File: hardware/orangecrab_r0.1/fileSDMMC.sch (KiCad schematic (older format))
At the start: 1 part, among them J4 MicroSD

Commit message: Update schematic
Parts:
- J4: symbol bosonFrameGrabber-rescue:Conn_01x11_Male-conn -> Connector:Conn_01x11_Male
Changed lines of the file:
@@
 $Descr A4 11693 8268
 encoding utf-8
-Sheet 4 5
+Sheet 4 6
 Title ""
 Date ""
@@
 $EndComp
 $Comp
-L bosonFrameGrabber-rescue:Conn_01x11_Male-conn J4
+L Connector:Conn_01x11_Male J4
 U 1 1 5AC0A68B
 P 5650 3850

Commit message: Routed more FPGA signals
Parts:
- J4: footprint bosonFrameGrabber:1040310811 -> gkl_conn:molex_microsd_1040310811
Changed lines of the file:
@@
 F 0 "J4" H 5450 4600 50  0000 C CNN
 F 1 "MicroSD" H 5400 4500 50  0000 C CNN
-F 2 "bosonFrameGrabber:1040310811" H 5650 3850 50  0001 C CNN
+F 2 "gkl_conn:molex_microsd_1040310811" H 5650 3850 50  0001 C CNN
 F 3 "~" H 5650 3850 50  0001 C CNN
 F 4 " WM6357CT-ND" H 5650 3850 60  0001 C CNN "SN-DK"

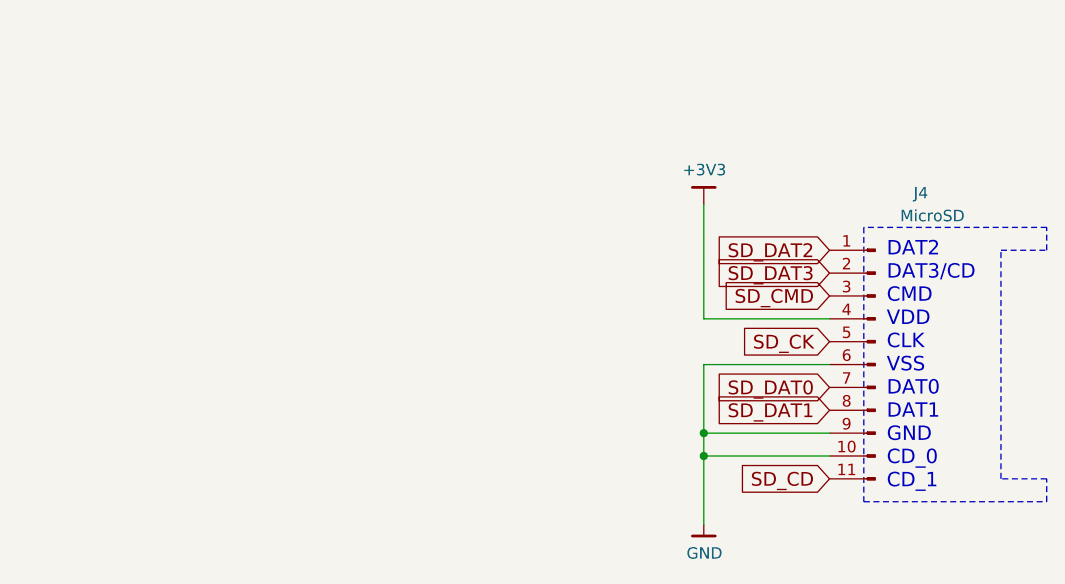
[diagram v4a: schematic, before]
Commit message: Added loads of decoupling capacitors. Added SD card. Started planning out power plane
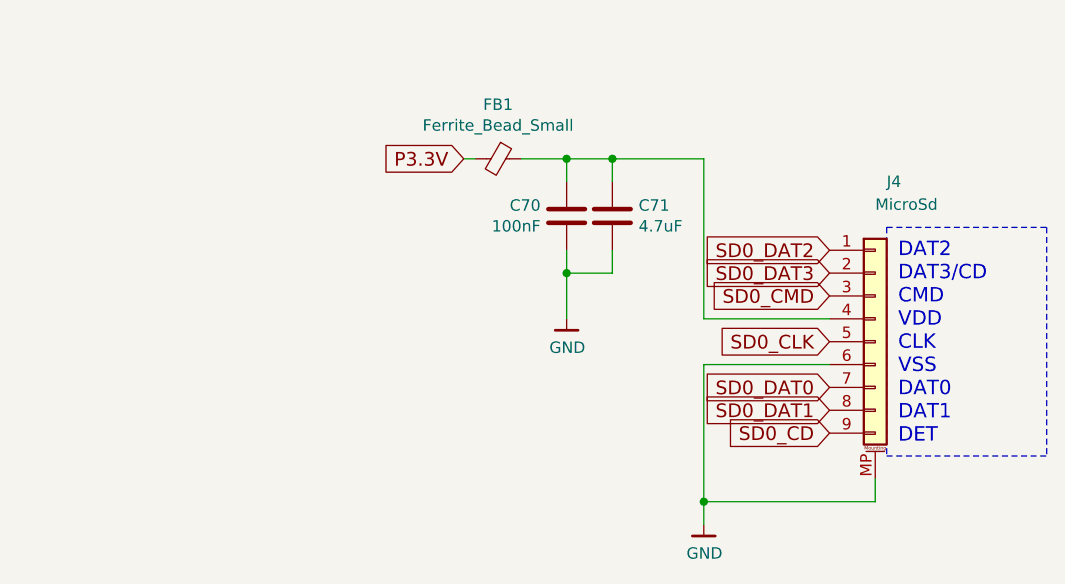
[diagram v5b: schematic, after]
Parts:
- removed J4: MicroSD, gkl_conn:molex_microsd_1040310811, symbol Connector:Conn_01x11_Male
- added C70: 100nF, Capacitor_SMD:C_0201_0603Metric, symbol Device:C
- added C71: 4.7uF, Capacitor_SMD:C_0603_1608Metric, symbol Device:C
- added FB1: Ferrite_Bead_Small, Inductor_SMD:L_0402_1005Metric, symbol Device:Ferrite_Bead_Small
- added J4: MicroSd, gkl_conn:micro_sd_1051620001, symbol Connector_Generic_MountingPin:Conn_01x09_MountingPin
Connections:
- net GND: now also C70.1, C71.2, J4.6 (Pin_6), J4.MP (MountPin)
- new net: C70.2, C71.1, FB1.1, J4.4 (Pin_4)
- new net P3.3V: FB1.2
- new net SD0_CD: J4.9 (Pin_9)
- new net SD0_CLK: J4.5 (Pin_5)
- new net SD0_CMD: J4.3 (Pin_3)
- new net SD0_DAT0: J4.7 (Pin_7)
- new net SD0_DAT1: J4.8 (Pin_8)
- new net SD0_DAT2: J4.1 (Pin_1)
- new net SD0_DAT3: J4.2 (Pin_2)
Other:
- note added: "DAT2\nDAT3/CD\nCMD\nVDD\nCLK\nVSS\nDAT0\nDAT1\nDET"
- note removed: "DAT2\nDAT3/CD\nCMD\nVDD\nCLK\nVSS\nDAT0\nDAT1\nGND\nCD_0\nCD_1\n"
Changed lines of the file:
@@
 $Descr A4 11693 8268
 encoding utf-8
-Sheet 4 6
+Sheet 4 7
 Title "Orange Crab"
 Date "2019-06-28"
@@
 $EndDescr
 Text GLabel 5450 3950 0    60   Input ~ 0
-SD_DAT0
+SD0_DAT0
 Text GLabel 5450 4050 0    60   Input ~ 0
-SD_DAT1
+SD0_DAT1
 Text GLabel 5450 3350 0    60   Input ~ 0
-SD_DAT2
+SD0_DAT2
 Text GLabel 5450 3450 0    60   Input ~ 0
-SD_DAT3
+SD0_DAT3
 Text GLabel 5450 3550 0    60   Input ~ 0
-SD_CMD
+SD0_CMD
 Text GLabel 5450 3750 0    60   Input ~ 0
-SD_CK
-Text GLabel 5450 4350 0    60   Input ~ 0
-SD_CD
-$Comp
-L gkl_power:+3V3 #PWR049
-U 1 1 5AC0A2E2
-P 4900 3150
-F 0 "#PWR049" H 4900 3000 50  0001 C CNN
-F 1 "+3V3" H 4903 3301 50  0000 C CNN
-F 2 "" H 4900 3150 50  0001 C CNN
-F 3 "" H 4900 3150 50  0001 C CNN
-	1    4900 3150
-	1    0    0    -1
-$EndComp
+SD0_CLK
+Text GLabel 5450 4150 0    60   Input ~ 0
+SD0_CD
 $Comp
 L gkl_power:GND #PWR050
@@
 	1    0    0    -1
 $EndComp
-$Comp
-L Connector:Conn_01x11_Male J4
-U 1 1 5AC0A68B
-P 5650 3850
-F 0 "J4" H 5450 4600 50  0000 C CNN
-F 1 "MicroSD" H 5400 4500 50  0000 C CNN
-F 2 "gkl_conn:molex_microsd_1040310811" H 5650 3850 50  0001 C CNN
-F 3 "~" H 5650 3850 50  0001 C CNN
-F 4 " WM6357CT-ND" H 5650 3850 60  0001 C CNN "SN-DK"
-F 5 "1040310811" H 0   0   50  0001 C CNN "PN"
-	1    5650 3850
-	-1   0    0    -1
-$EndComp
-Wire Wire Line
-	4900 3850 4900 4150
-Wire Wire Line
-	4900 4150 5450 4150
-Text Notes 5700 4400 0    63   ~ 0
-DAT2\nDAT3/CD\nCMD\nVDD\nCLK\nVSS\nDAT0\nDAT1\nGND\nCD_0\nCD_1\n
+Text Notes 5750 4200 0    63   ~ 0
+DAT2\nDAT3/CD\nCMD\nVDD\nCLK\nVSS\nDAT0\nDAT1\nDET
 Wire Notes Line
-	5600 3250 5600 4450
-Wire Notes Line
-	5600 4450 6400 4450
-Wire Notes Line
-	6400 4450 6400 4350
-Wire Notes Line
-	6400 4350 6200 4350
-Wire Notes Line
-	6200 4350 6200 3350
-Wire Notes Line
-	6200 3350 6400 3350
-Wire Notes Line
-	6400 3350 6400 3250
-Wire Notes Line
-	6400 3250 5600 3250
+	5700 3250 5700 4250
 Wire Wire Line
 	5450 3650 4900 3650
 Wire Wire Line
-	4900 3650 4900 3150
+	5450 3850 4900 3850
+$Comp
+L Connector_Generic_MountingPin:Conn_01x09_MountingPin J4
+U 1 1 5D5BA533
+P 5650 3750
+F 0 "J4" H 5700 4450 50  0000 L CNN
+F 1 "MicroSd" H 5650 4350 50  0000 L CNN
+F 2 "gkl_conn:micro_sd_1051620001" H 5650 3750 50  0001 C CNN
+F 3 "~" H 5650 3750 50  0001 C CNN
+F 4 "1051620001" H 5650 3750 50  0001 C CNN "PN"
+F 5 "Molex" H 5650 3750 50  0001 C CNN "Mfg"
+	1    5650 3750
+	1    0    0    -1
+$EndComp
 Wire Wire Line
-	5450 3850 4900 3850
-Connection ~ 4900 4150
+	4900 3850 4900 4450
 Wire Wire Line
-	4900 4150 4900 4250
+	5650 4350 5650 4450
 Wire Wire Line
-	5450 4250 4900 4250
-Connection ~ 4900 4250
+	5650 4450 4900 4450
+Connection ~ 4900 4450
 Wire Wire Line
-	4900 4250 4900 4550
+	4900 4450 4900 4550
+Wire Notes Line
+	5700 4250 6400 4250
+Wire Notes Line
+	6400 3250 6400 4250
+Wire Notes Line
+	5700 3250 6400 3250
+Text GLabel 3850 2950 0    60   Input ~ 0
+P3.3V
+$Comp
+L Device:Ferrite_Bead_Small FB1
+U 1 1 5D5BE84B
+P 4000 2950
+F 0 "FB1" V 3763 2950 50  0000 C CNN
+F 1 "Ferrite_Bead_Small" V 3854 2950 50  0000 C CNN
+F 2 "Inductor_SMD:L_0402_1005Metric" V 3930 2950 50  0001 C CNN
+F 3 "~" H 4000 2950 50  0001 C CNN
+	1    4000 2950
+	0    1    1    0
+$EndComp
+$Comp
+L Device:C C71
+U 1 1 5D5BF142
+P 4500 3200
+F 0 "C71" H 4615 3246 50  0000 L CNN
+F 1 "4.7uF" H 4615 3155 50  0000 L CNN
+F 2 "Capacitor_SMD:C_0603_1608Metric" H 4538 3050 50  0001 C CNN
+F 3 "~" H 4500 3200 50  0001 C CNN
+	1    4500 3200
+	1    0    0    -1
+$EndComp
+$Comp
+L Device:C C70
+U 1 1 5D5BF444
+P 4300 3200
+F 0 "C70" H 4186 3154 50  0000 R CNN
+F 1 "100nF" H 4186 3245 50  0000 R CNN
+F 2 "Capacitor_SMD:C_0201_0603Metric" H 4338 3050 50  0001 C CNN
+F 3 "~" H 4300 3200 50  0001 C CNN
+	1    4300 3200
+	1    0    0    1
+$EndComp
+Wire Wire Line
+	4100 2950 4300 2950
+Wire Wire Line
+	4900 2950 4900 3650
+Wire Wire Line
+	4500 3050 4500 2950
+Connection ~ 4500 2950
+Wire Wire Line
+	4500 2950 4900 2950
+Wire Wire Line
+	4300 3050 4300 2950
+Connection ~ 4300 2950
+Wire Wire Line
+	4300 2950 4500 2950
+Wire Wire Line
+	3900 2950 3850 2950
+Wire Wire Line
+	4300 3350 4300 3450
+Wire Wire Line
+	4500 3350 4500 3450
+Wire Wire Line
+	4500 3450 4300 3450
+Connection ~ 4300 3450
+Wire Wire Line
+	4300 3450 4300 3650
+$Comp
+L gkl_power:GND #PWR0159
+U 1 1 5D5C1FC1
+P 4300 3650
+F 0 "#PWR0159" H 4300 3400 50  0001 C CNN
+F 1 "GND" H 4303 3524 50  0000 C CNN
+F 2 "" H 4200 3300 50  0001 C CNN
+F 3 "" H 4300 3650 50  0001 C CNN
+	1    4300 3650
+	1    0    0    -1
+$EndComp
 $EndSCHEMATC

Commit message: Added pulldown on TS pin to disable TS func. Added 4.7uF cap to USB input. Corrected Battery polarity Calculated correct DCDC Fb Added pullup to SWCLK Added Pulldown to TCK Added Pinout legend on top layer Fixed Missing VCC on Flash Neaten up Power Plane Schematic Checklist complete.
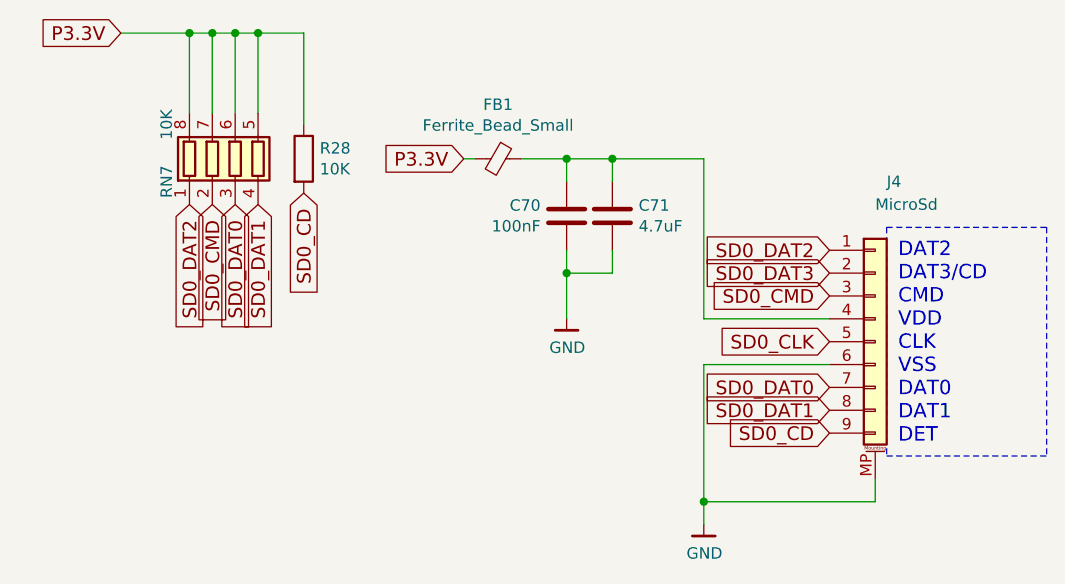
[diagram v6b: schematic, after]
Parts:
- added R28: 10K, Resistor_SMD:R_0201_0603Metric, symbol Device:R
- added RN7: 10K, Resistor_SMD:R_Array_Convex_4x0402, symbol Device:R_Pack04
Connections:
- net P3.3V: now also R28.1, RN7.5 (R4.2), RN7.6 (R3.2), RN7.7 (R2.2), RN7.8 (R1.2)
- net SD0_CD: now also R28.2
- net SD0_CMD: now also RN7.2 (R2.1)
- net SD0_DAT0: now also RN7.3 (R3.1)
- net SD0_DAT1: now also RN7.4 (R4.1)
- net SD0_DAT2: now also RN7.1 (R1.1)
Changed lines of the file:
@@
 	1    0    0    -1
 $EndComp
+$Comp
+L Device:R_Pack04 RN?
+U 1 1 5D5ABE41
+P 2850 2950
+AR Path="/5ABD38F2/5D5ABE41" Ref="RN?"  Part="1"
+AR Path="/5AC0A2A0/5D5ABE41" Ref="RN7"  Part="1"
+F 0 "RN7" V 2550 2850 50  0000 C CNN
+F 1 "10K" V 2550 3100 50  0000 C CNN
+F 2 "Resistor_SMD:R_Array_Convex_4x0402" V 3125 2950 50  0001 C CNN
+F 3 "~" H 2850 2950 50  0001 C CNN
+F 4 "CRA06S08349R9FTA" H 2850 2950 50  0001 C CNN "PN"
+	1    2850 2950
+	1    0    0    -1
+$EndComp
+Text GLabel 2350 2400 0    60   Input ~ 0
+P3.3V
+Wire Wire Line
+	2350 2400 2650 2400
+Wire Wire Line
+	2650 2400 2650 2750
+Wire Wire Line
+	2650 2400 2750 2400
+Wire Wire Line
+	2750 2400 2750 2750
+Connection ~ 2650 2400
+Wire Wire Line
+	2750 2400 2850 2400
+Wire Wire Line
+	2850 2400 2850 2750
+Connection ~ 2750 2400
+Wire Wire Line
+	2850 2400 2950 2400
+Wire Wire Line
+	2950 2400 2950 2750
+Connection ~ 2850 2400
+Text GLabel 2650 3150 3    60   Input ~ 0
+SD0_DAT2
+Text GLabel 2750 3150 3    60   Input ~ 0
+SD0_CMD
+Text GLabel 2850 3150 3    60   Input ~ 0
+SD0_DAT0
+Text GLabel 2950 3150 3    60   Input ~ 0
+SD0_DAT1
+$Comp
+L Device:R R28
+U 1 1 5D5AD51E
+P 3150 2950
+F 0 "R28" H 3220 2996 50  0000 L CNN
+F 1 "10K" H 3220 2905 50  0000 L CNN
+F 2 "Resistor_SMD:R_0201_0603Metric" V 3080 2950 50  0001 C CNN
+F 3 "~" H 3150 2950 50  0001 C CNN
+	1    3150 2950
+	1    0    0    -1
+$EndComp
+Text GLabel 3150 3100 3    60   Input ~ 0
+SD0_CD
+Wire Wire Line
+	2950 2400 3150 2400
+Wire Wire Line
+	3150 2400 3150 2800
+Connection ~ 2950 2400
 $EndSCHEMATC

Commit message: Rerouted User Io to provide a common connector. Diff pairs routed. Updated gkl to include new connector. Removed old test points Removed JTAG test points on bottom layer. Moved micro SD card Moved some components to provide space for ul marking.
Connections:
- net SD0_CMD: now also RN7.3 (R3.1); no longer RN7.2 (R2.1)
- net SD0_DAT0: now also RN7.2 (R2.1); no longer RN7.3 (R3.1)
- net SD0_DAT1: now also RN7.1 (R1.1); no longer RN7.4 (R4.1)
- net SD0_DAT2: now also RN7.4 (R4.1); no longer RN7.1 (R1.1)
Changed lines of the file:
@@
 	2950 2400 2950 2750
 Connection ~ 2850 2400
+Text GLabel 2950 3150 3    60   Input ~ 0
+SD0_DAT2
+Text GLabel 2850 3150 3    60   Input ~ 0
+SD0_CMD
+Text GLabel 2750 3150 3    60   Input ~ 0
+SD0_DAT0
 Text GLabel 2650 3150 3    60   Input ~ 0
-SD0_DAT2
-Text GLabel 2750 3150 3    60   Input ~ 0
-SD0_CMD
-Text GLabel 2850 3150 3    60   Input ~ 0
-SD0_DAT0
-Text GLabel 2950 3150 3    60   Input ~ 0
 SD0_DAT1
 $Comp

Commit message: Updated BOM fields in KiCad project Exported ibom Clarify fab notes
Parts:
- C70: Mfg (none) -> Samsung Electro-Mechanics; PN (none) -> CL03A104KQ3NNNC
- C71: Mfg (none) -> Samsung Electro-Mechanics; PN (none) -> CL10A475KP8NNNC
- FB1: value Ferrite_Bead_Small -> 600R; Mfg (none) -> Murata Electronics North America; PN (none) -> BLM15AG601SN1D
- R28: Mfg (none) -> ‎Yageo‎; PN (none) -> RC0201FR-0710KL
- RN7: Mfg (none) -> Vishay Dale; PN CRA06S08349R9FTA -> CRA06S08310K0JTA
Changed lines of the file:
@@
 P 4000 2950
 F 0 "FB1" V 3763 2950 50  0000 C CNN
-F 1 "Ferrite_Bead_Small" V 3854 2950 50  0000 C CNN
+F 1 "600R" V 3854 2950 50  0000 C CNN
 F 2 "Inductor_SMD:L_0402_1005Metric" V 3930 2950 50  0001 C CNN
 F 3 "~" H 4000 2950 50  0001 C CNN
+F 4 "Murata Electronics North America" H 4000 2950 50  0001 C CNN "Mfg"
+F 5 "BLM15AG601SN1D" H 4000 2950 50  0001 C CNN "PN"
 	1    4000 2950
 	0    1    1    0
@@
 F 2 "Capacitor_SMD:C_0603_1608Metric" H 4538 3050 50  0001 C CNN
 F 3 "~" H 4500 3200 50  0001 C CNN
+F 4 "Samsung Electro-Mechanics" H 4500 3200 50  0001 C CNN "Mfg"
+F 5 "CL10A475KP8NNNC" H 4500 3200 50  0001 C CNN "PN"
 	1    4500 3200
 	1    0    0    -1
@@
 F 2 "Capacitor_SMD:C_0201_0603Metric" H 4338 3050 50  0001 C CNN
 F 3 "~" H 4300 3200 50  0001 C CNN
+F 4 "Samsung Electro-Mechanics" H 4300 3200 50  0001 C CNN "Mfg"
+F 5 "CL03A104KQ3NNNC" H 4300 3200 50  0001 C CNN "PN"
 	1    4300 3200
 	1    0    0    1
@@
 F 2 "Resistor_SMD:R_Array_Convex_4x0402" V 3125 2950 50  0001 C CNN
 F 3 "~" H 2850 2950 50  0001 C CNN
-F 4 "CRA06S08349R9FTA" H 2850 2950 50  0001 C CNN "PN"
+F 4 "CRA06S08310K0JTA" H 2850 2950 50  0001 C CNN "PN"
+F 5 "Vishay Dale" H 2850 2950 50  0001 C CNN "Mfg"
 	1    2850 2950
 	1    0    0    -1
@@
 F 2 "Resistor_SMD:R_0201_0603Metric" V 3080 2950 50  0001 C CNN
 F 3 "~" H 3150 2950 50  0001 C CNN
+F 4 "‎Yageo‎" H 3150 2950 50  0001 C CNN "Mfg"
+F 5 "RC0201FR-0710KL" H 3150 2950 50  0001 C CNN "PN"
 	1    3150 2950
 	1    0    0    -1
